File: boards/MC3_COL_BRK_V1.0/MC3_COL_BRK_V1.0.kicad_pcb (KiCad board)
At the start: 2 copper layers, 0 parts

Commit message: MC3_COL_BRK: drop test points — every net is probeable on THT XH pins; ERC clean
Co-Authored-By: Claude Fable 5 <noreply@anthropic.com>
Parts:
- added D1: PWR_LED, MC3_COL_BRK:LED_0603_1608Metric, F.Cu at (134.6, 100.8)
- added H1: M2, MC3_COL_BRK:MountingHole_2.2mm_M2, F.Cu at (133.4, 92.8)
- added H2: M2, MC3_COL_BRK:MountingHole_2.2mm_M2, F.Cu at (133.6, 108.0)
- added J1: HARNESS_FFC_6P, MC3_COL_BRK:TE_84952-6_1x06-1MP_P1.0mm_Horizontal, B.Cu at (88.0, 95.0)
- added J2: PWR_IN, MC3_COL_BRK:JST_XH_B2B-XH-A_1x02_P2.50mm_Vertical, B.Cu at (98.8, 100.8)
- added J3: PWR_OUT, MC3_COL_BRK:JST_XH_B2B-XH-A_1x02_P2.50mm_Vertical, B.Cu at (107.6, 100.8)
- added J4: CAN_IN, MC3_COL_BRK:JST_XH_B3B-XH-A_1x03_P2.50mm_Vertical, F.Cu at (109.1, 106.4)
- added J5: CAN_OUT, MC3_COL_BRK:JST_XH_B3B-XH-A_1x03_P2.50mm_Vertical, F.Cu at (97.3, 106.4)
- added J6: YAW_MOTOR, MC3_COL_BRK:JST_XH_B2B-XH-A_1x02_P2.50mm_Vertical, F.Cu at (83.4, 103.9)
- added R1: 120R, MC3_COL_BRK:R_0603_1608Metric, F.Cu at (114.6, 98.4)
- added R2: 10k, MC3_COL_BRK:R_0603_1608Metric, F.Cu at (114.6, 100.9)
- added SW1: CAN_TERM, MC3_COL_BRK:SW_DIP_SPSTx01_Slide_6.7x4.1mm_W8.61mm_P2.54mm_LowProfile, F.Cu at (104.4, 95.2)
- added TP1: VIN, MC3_COL_BRK:TestPoint_Pad_1.0x1.0mm, F.Cu at (128.1, 81.2)
- added TP2: GND, MC3_COL_BRK:TestPoint_Pad_1.0x1.0mm, F.Cu at (128.1, 84.2)
- added TP3: CANH, MC3_COL_BRK:TestPoint_Pad_1.0x1.0mm, F.Cu at (131.2, 81.2)
- added TP4: CANL, MC3_COL_BRK:TestPoint_Pad_1.0x1.0mm, F.Cu at (131.2, 84.2)
- added TP5: YAW_OUT1, MC3_COL_BRK:TestPoint_Pad_1.0x1.0mm, F.Cu at (134.2, 81.2)
- added TP6: YAW_OUT2, MC3_COL_BRK:TestPoint_Pad_1.0x1.0mm, F.Cu at (134.2, 84.2)
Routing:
- net /CANL: track 0.00 -> 38.6 mm
- net /CANH: track 0.00 -> 30.4 mm
- net /VIN: track 0.00 -> 26.1 mm
- net /YAW_OUT1: track 0.00 -> 18.1 mm, vias 0 -> 1
- net /YAW_OUT2: track 0.00 -> 15.3 mm, vias 0 -> 1
- added copper zone on B.Cu, net /GND
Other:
- board outline added: 40 x 20 mm

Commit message: MC3_COL_BRK: provisional 40x20 outline, footprints imported, placement WIP
Co-Authored-By: Claude Fable 5 <noreply@anthropic.com>
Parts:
- removed TP1: VIN, MC3_COL_BRK:TestPoint_Pad_1.0x1.0mm
- removed TP2: GND, MC3_COL_BRK:TestPoint_Pad_1.0x1.0mm
- removed TP3: CANH, MC3_COL_BRK:TestPoint_Pad_1.0x1.0mm
- removed TP4: CANL, MC3_COL_BRK:TestPoint_Pad_1.0x1.0mm
- removed TP5: YAW_OUT1, MC3_COL_BRK:TestPoint_Pad_1.0x1.0mm
- removed TP6: YAW_OUT2, MC3_COL_BRK:TestPoint_Pad_1.0x1.0mm
- moved D1 24.0 mm to (110.8, 98.0), turned to 180 degrees
- moved SW1 12.8 mm to (116.2, 100.2), turned to -90 degrees
- moved R1 7.61 mm to (113.0, 105.8), turned to 90 degrees
- moved R2 7.57 mm to (107.6, 98.0)
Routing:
- net /CANL: track 38.6 -> 52.3 mm
- net Net-(SW1-A): track 0.00 -> 11.2 mm
- net /CANH: track 30.4 -> 34.4 mm
- net /YAW_OUT2: track 15.3 -> 19.3 mm
- net /GND: track 0.00 -> 3.72 mm
- net /VIN: track 26.1 -> 29.3 mm
- net Net-(D1-A): track 0.00 -> 1.58 mm
- net /YAW_OUT1: track 18.1 -> 16.6 mm

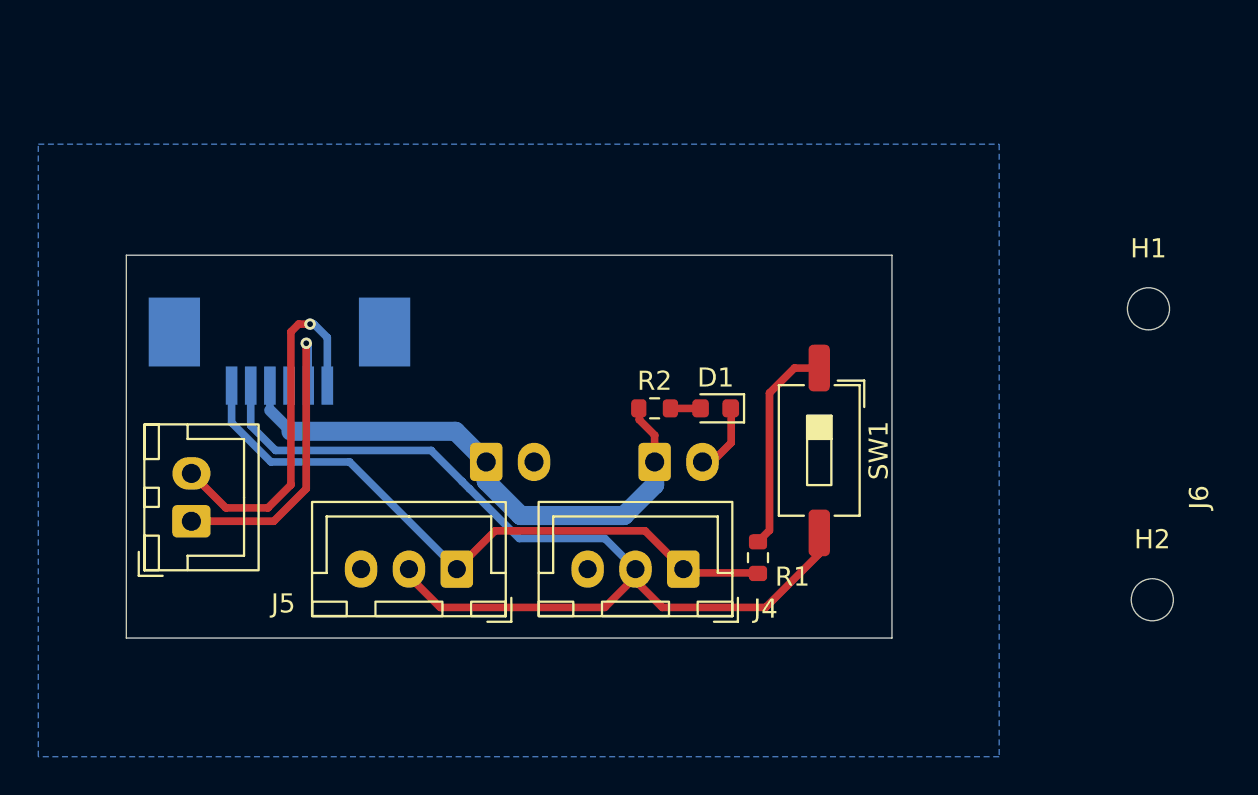
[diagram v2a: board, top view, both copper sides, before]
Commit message: MC3_COL_BRK: FFC rear courtyard/silk walked back for edge-overhang mounting; H3 third M2 hole added
Co-Authored-By: Claude Fable 5 <noreply@anthropic.com>
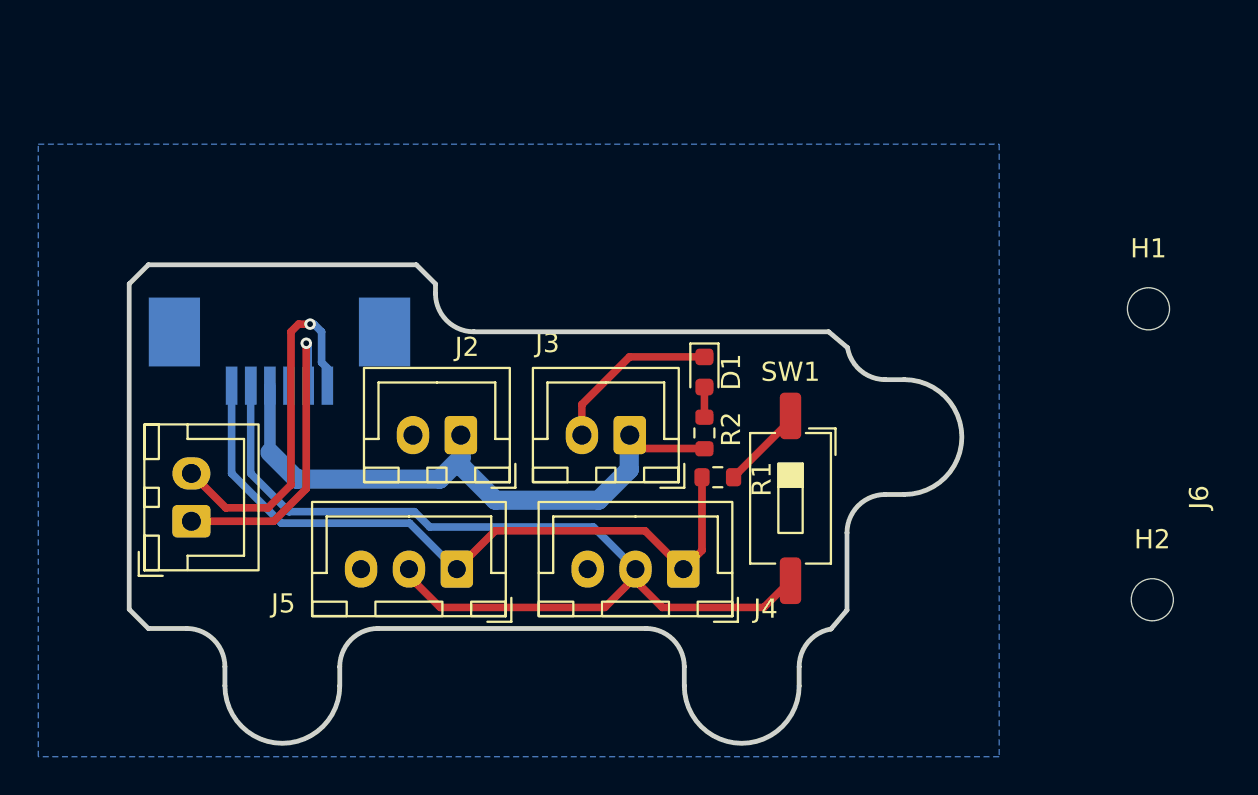
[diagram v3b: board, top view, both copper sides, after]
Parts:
- J2, J3: moved to F.Cu
- moved R1 4.70 mm to (110.9, 101.6), turned to 0 degrees
- moved SW1 2.92 mm to (114.7, 102.7)
- moved R2 2.90 mm to (110.2, 99.3), turned to 90 degrees
- moved D1 1.99 mm to (110.2, 96.1), turned to -90 degrees
- moved J2 1.93 mm to (97.5, 99.4), turned to 180 degrees
- moved J3 1.91 mm to (106.3, 99.4), turned to 180 degrees
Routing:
- net Net-(SW1-A): track 11.2 -> 4.44 mm
- net /GND: track 3.72 -> 9.03 mm
- net /VIN: track 29.3 -> 33.5 mm
- net /CANH: track 34.4 -> 37.1 mm
- net /CANL: track 52.3 -> 50.6 mm
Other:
- board size 40 x 20 mm -> 43.5 x 25 mm

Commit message: MC3_COL_BRK: J1 updated to overhang footprint, H3 placed, outline from CAD DXF
Co-Authored-By: Claude Fable 5 <noreply@anthropic.com>
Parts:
- added H3: M2, MC3_COL_BRK:MountingHole_2.2mm_M2, F.Cu at (120.7, 99.5)
- moved H2 45.7 mm to (88.2, 112.5)
- moved H1 29.0 mm to (112.2, 112.5)
- moved SW1 0.30 mm to (115.0, 102.7)
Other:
- board text added: "+"
- board text added: "-"
- board text added: "CANH CANL GND"
